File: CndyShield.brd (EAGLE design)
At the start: 69.9 x 78.1 mm, 31 parts, among them U1 ARDUINOR3-BPLACE

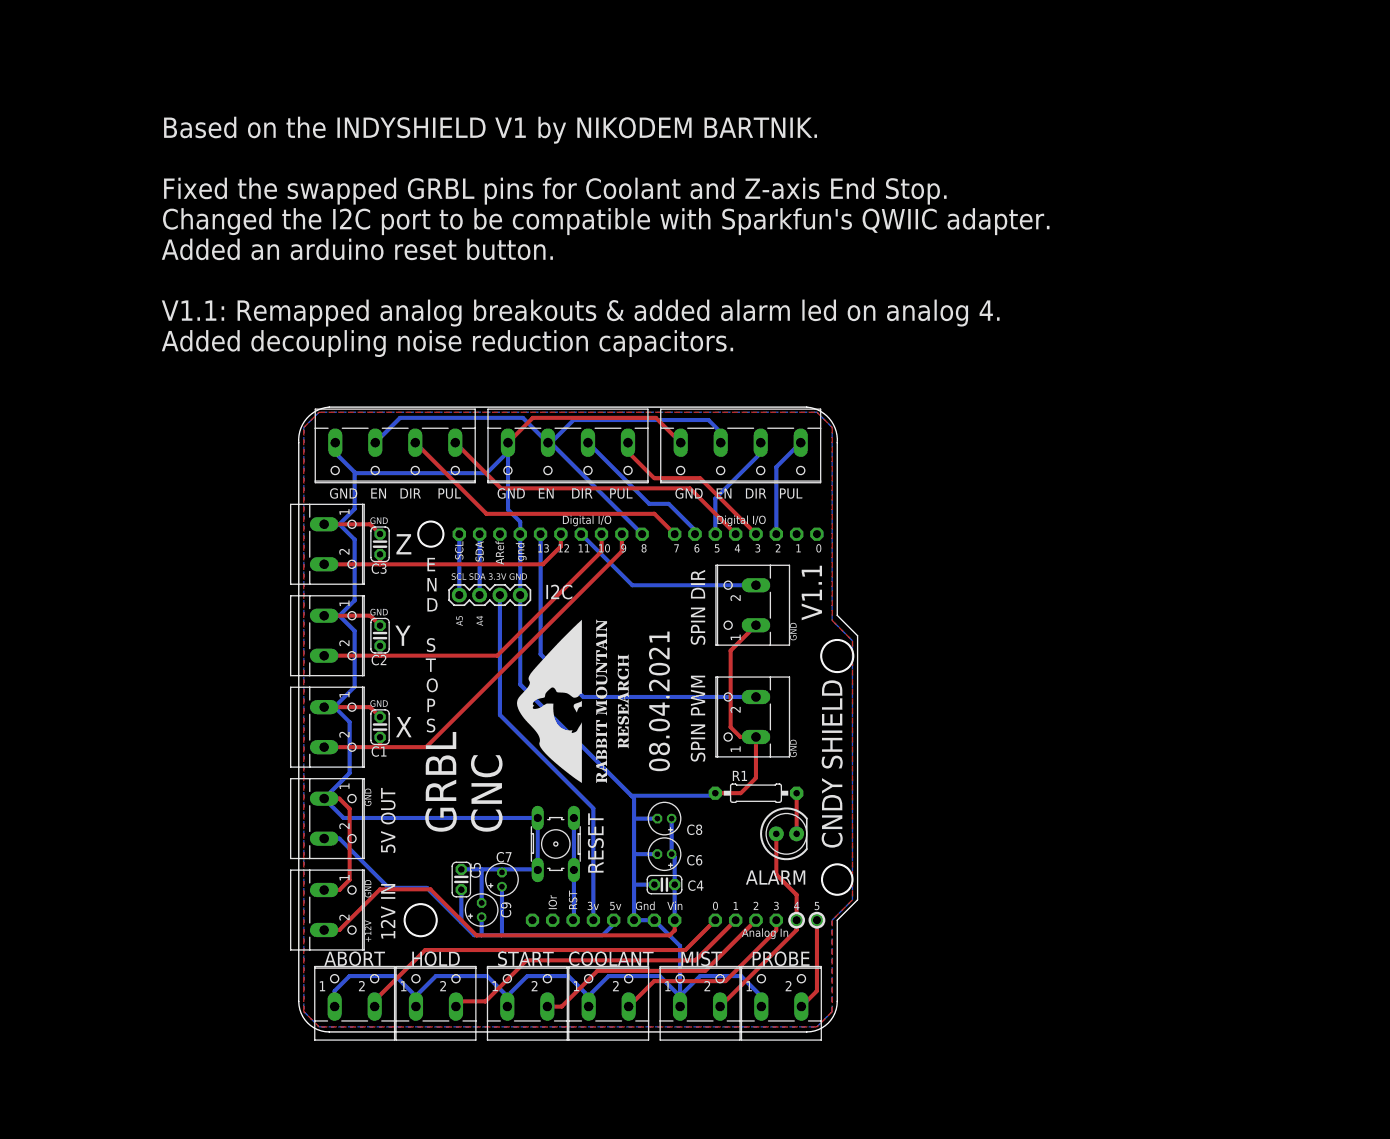
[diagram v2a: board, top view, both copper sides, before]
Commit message: Add files via upload
V1.2: Fixed swapped silkscreen text for Spindle PWM and Spindle Direction. Added optional LED to Spindle PWM (pin 11) as an optional safety warning light.
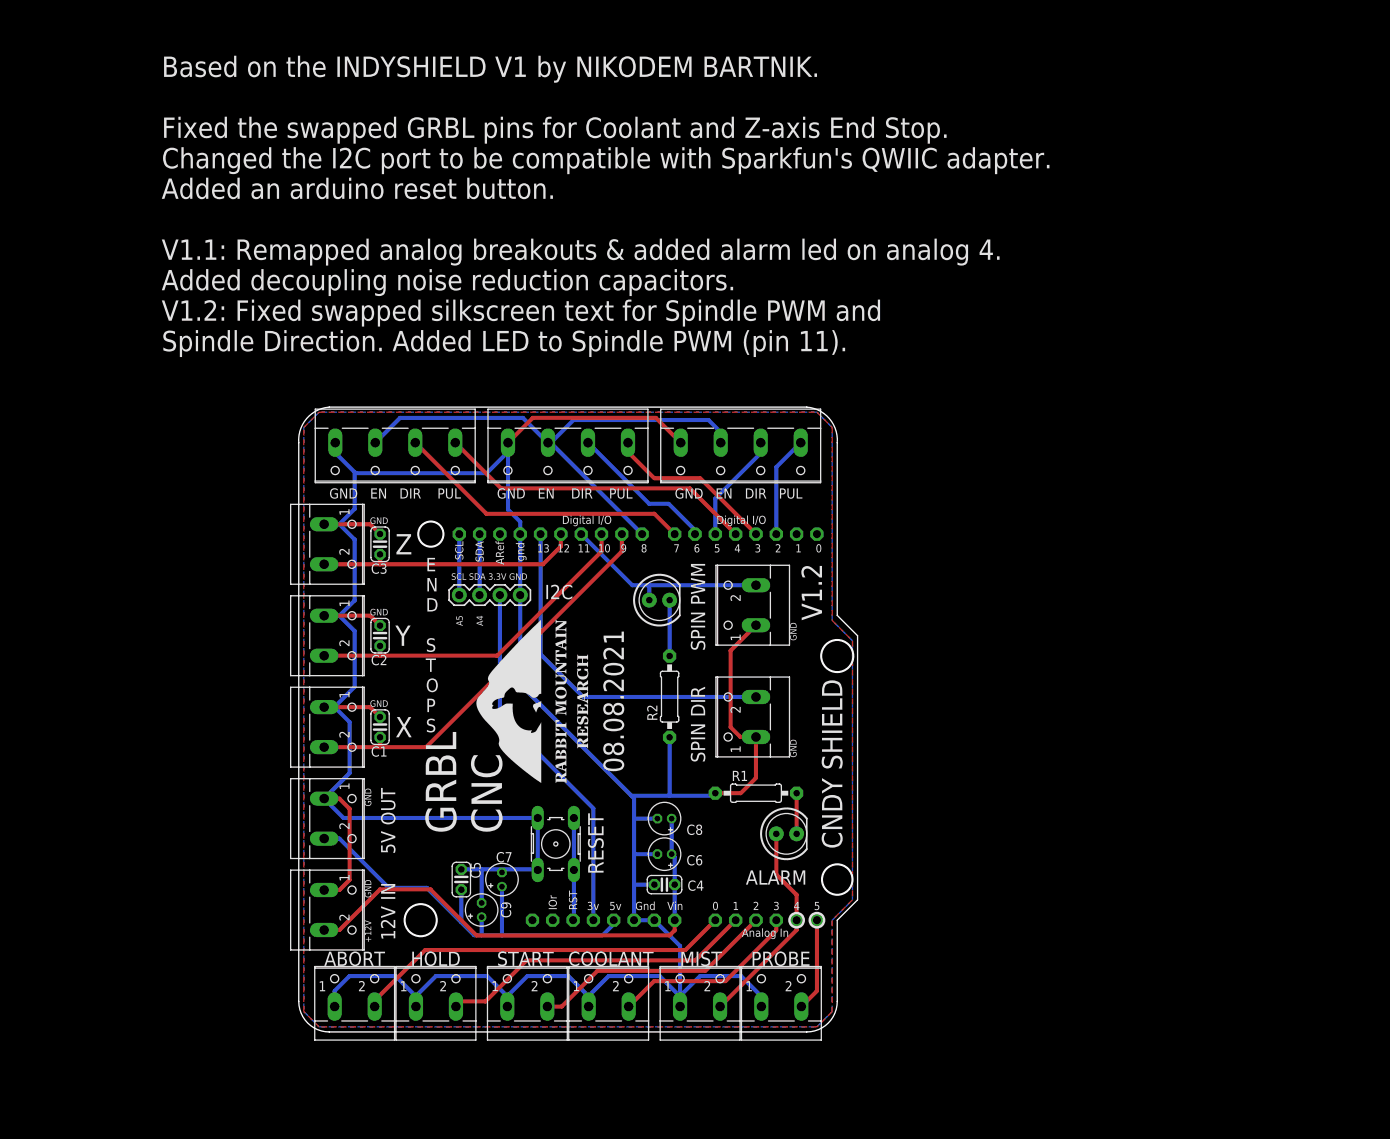
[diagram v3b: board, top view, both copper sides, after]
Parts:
- added D2: (no value), SparkFun-LED:LED_5MM
- added R2: 330, adafruit:0207/10
- moved U$2 5.08 mm to (71.8, 42.5)
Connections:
- new net N$11: D2.K, R2.2
- net GND: now also R2.1
- net SPIN_E: now also D2.A
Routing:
- net GND: track 395.3 -> 402.6 mm
- net N$11: track 0.00 -> 6.98 mm
- net SPIN_E: track 24.5 -> 26.4 mm
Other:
- board text added: "08.08.2021"
- board text added: "Based on the INDYSHIELD V1 by NIKODEM BARTNIK. Fixed the swapped GRBL pins for Coolant and Z-axis End Stop. Changed the I2C port to be compatible with Sparkfun's QWIIC adapter. Added an arduino reset button. V1.1: Remapped analog breakouts & added alarm led on analog 4. Added decoupling noise reduction capacitors. V1.2: Fixed swapped silkscreen text for Spindle PWM and Spindle Direction. Added LE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"
- board text added: "V1.2"
- board text removed: "08.04.2021"
- board text removed: "Based on the INDYSHIELD V1 by NIKODEM BARTNIK. Fixed the swapped GRBL pins for Coolant and Z-axis End Stop. Changed the I2C port to be compatible with Sparkfun's QWIIC adapter. Added an arduino reset button. V1.1: Remapped analog breakouts & added alarm led on analog 4. Added decoupling noise reduction capacitors."
- board text removed: "V1.1"
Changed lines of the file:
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@@
 Added an arduino reset button.
 V1.1: Remapped analog breakouts &amp; added alarm led on analog 4.
-Added decoupling noise reduction capacitors.</text>
-<text x="81.915" y="43.815" size="2.54" layer="25" rot="R90">08.04.2021</text>
+Added decoupling noise reduction capacitors.
+V1.2: Fixed swapped silkscreen text for Spindle PWM and
+Spindle Direction. Added LED to Spindle PWM (pin 11).</text>
+<text x="76.2" y="43.815" size="2.54" layer="25" rot="R90">08.08.2021</text>
 <text x="97.79" y="45.72" size="0.8128" layer="25" rot="R90">GND</text>
 <text x="97.79" y="60.325" size="0.8128" layer="25" rot="R90">GND</text>
@@
 CNC</text>
 <text x="73.66" y="31.115" size="1.9304" layer="21" font="vector" ratio="20" rot="R90">RESET</text>
-<text x="86.36" y="59.69" size="1.778" layer="21" font="vector" ratio="20" rot="R90">SPIN DIR</text>
+<text x="86.36" y="59.055" size="1.778" layer="21" font="vector" ratio="20" rot="R90">SPIN PWM</text>
 <text x="69.215" y="19.685" size="1.778" layer="21" font="vector" ratio="20">COOLANT</text>
 <text x="38.735" y="19.685" size="1.778" layer="21" font="vector" ratio="20">ABORT</text>
-<text x="86.36" y="45.085" size="1.778" layer="21" font="vector" ratio="20" rot="R90">SPIN PWM</text>
+<text x="86.36" y="45.085" size="1.778" layer="21" font="vector" ratio="20" rot="R90">SPIN DIR</text>
 <text x="103.505" y="34.29" size="2.54" layer="21" font="vector" ratio="20" rot="R90">CNDY SHIELD</text>
 <text x="49.53" y="19.685" size="1.778" layer="21" font="vector" ratio="20">HOLD</text>
@@
 <text x="83.185" y="19.685" size="1.778" layer="21" font="vector" ratio="20">MIST</text>
 <text x="92.075" y="19.685" size="1.778" layer="21" font="vector" ratio="20">PROBE</text>
-<text x="100.965" y="62.865" size="2.54" layer="21" font="vector" ratio="20" rot="R90">V1.1</text>
+<text x="100.965" y="62.865" size="2.54" layer="21" font="vector" ratio="20" rot="R90">V1.2</text>
 <text x="47.625" y="22.86" size="1.778" layer="21" font="vector" ratio="20" rot="R90">12V IN</text>
 <text x="47.625" y="33.655" size="1.778" layer="21" font="vector" ratio="20" rot="R90">5V OUT</text>
@@
 <attribute name="VALUE" x="62.611" y="37.973" size="1.27" layer="27" ratio="10" rot="R270"/>
 </element>
-<element name="U$2" library="RMR" package="RMR-SIT-14MM" value="" x="76.835" y="42.545" smashed="yes" rot="R90"/>
+<element name="U$2" library="RMR" package="RMR-SIT-14MM" value="" x="71.755" y="42.545" smashed="yes" rot="R90"/>
 <element name="COOL" library="con-wago-500" library_urn="urn:adsk.eagle:library:195" package="W237-102" package3d_urn="urn:adsk.eagle:package:10688/1" value="" x="74.295" y="15.875" smashed="yes">
 <attribute name="MF" value="" x="63.5" y="38.1" size="1.778" layer="27" display="off"/>
@@
 <attribute name="NAME" x="62.103" y="25.654" size="1.27" layer="25" ratio="10" rot="R90"/>
 <attribute name="VALUE" x="60.198" y="28.829" size="1.27" layer="27" ratio="10" rot="R90"/>
+</element>
+<element name="D2" library="SparkFun-LED" library_urn="urn:adsk.eagle:library:529" package="LED_5MM" package3d_urn="urn:adsk.eagle:package:39353/1" value="" x="80.645" y="65.405" smashed="yes">
+<attribute name="VALUE" x="80.6704" y="62.0141" size="0.6096" layer="27" font="vector" ratio="20" align="top-center"/>
+</element>
+<element name="R2" library="adafruit" library_urn="urn:adsk.eagle:library:420" package="0207/10" package3d_urn="urn:adsk.eagle:package:6240597/1" value="330" x="81.915" y="53.34" smashed="yes" rot="R90">
+<attribute name="NAME" x="80.391" y="50.292" size="1.27" layer="25" ratio="10" rot="R90"/>
+<attribute name="VALUE" x="82.55" y="51.0794" size="1.27" layer="27" ratio="10" rot="R90"/>
 </element>
 </elements>
@@
 <wire x1="83.225" y1="22.185" x2="83.225" y2="14.605" width="0.508" layer="16"/>
 <wire x1="87.63" y1="41.275" x2="87.3125" y2="40.9575" width="0.508" layer="16"/>
-<wire x1="87.3125" y1="40.9575" x2="77.1525" y2="40.9575" width="0.508" layer="16"/>
+<wire x1="87.3125" y1="40.9575" x2="81.915" y2="40.9575" width="0.508" layer="16"/>
 <contactref element="C1" pad="2"/>
 <contactref element="C2" pad="2"/>
 <contactref element="C3" pad="2"/>
+<wire x1="81.915" y1="40.9575" x2="77.1525" y2="40.9575" width="0.508" layer="16"/>
 <wire x1="45.72" y1="73.66" x2="44.49" y2="74.89" width="0.508" layer="1"/>
 <wire x1="44.49" y1="74.89" x2="38.735" y2="74.89" width="0.508" layer="1"/>
@@
 <wire x1="80.391" y1="38.1" x2="77.47" y2="38.1" width="0.508" layer="16"/>
 <wire x1="58.42" y1="27.559" x2="58.42" y2="31.75" width="0.508" layer="16"/>
+<contactref element="R2" pad="1"/>
+<wire x1="81.915" y1="48.26" x2="81.915" y2="40.9575" width="0.508" layer="16"/>
 </signal>
 <signal name="S_EN">
@@
 <contactref element="U1" pad="D11"/>
 <wire x1="77.256" y1="67.27" x2="70.866" y2="73.66" width="0.508" layer="16"/>
-<wire x1="92.71" y1="67.27" x2="77.256" y2="67.27" width="0.508" layer="16"/>
+<wire x1="92.71" y1="67.27" x2="79.375" y2="67.27" width="0.508" layer="16"/>
+<contactref element="D2" pad="A"/>
+<wire x1="79.375" y1="67.27" x2="77.256" y2="67.27" width="0.508" layer="16"/>
+<wire x1="79.375" y1="65.405" x2="79.375" y2="67.27" width="0.508" layer="16"/>
 </signal>
 <signal name="SPIN_DIR">
@@
 <wire x1="97.79" y1="36.195" x2="97.79" y2="41.275" width="0.508" layer="1"/>
 </signal>
+<signal name="N$11">
+<contactref element="D2" pad="K"/>
+<contactref element="R2" pad="2"/>
+<wire x1="81.915" y1="65.405" x2="81.915" y2="58.42" width="0.508" layer="16"/>
+</signal>
 </signals>

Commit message: Add files via upload
V1.3 Updated Silkscreen. Added OSHW Logo. Noise reduction caps.
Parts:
- added C10, C11, C12, C13: (no value), adafruit:C025-024X044
- added U$1: (no value), RMR:OSHW-LOGO-M
- moved U$2 1.42 mm to (73.0, 41.9)
- moved D1 1.27 mm to (96.5, 37.5)
- moved R1 1.27 mm to (92.7, 42.5)
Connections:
- new net MIST: D1.A, U1.A4
- net ABORT: now also C10.1
- net GND: now also C10.2, C11.2, C12.2, C13.2
- net HOLD: now also C11.1
- net LIGHT: no longer D1.A, U1.A4
- net PROBE: now also C13.1
- net START: now also C12.1
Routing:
- net GND: track 402.6 -> 423.0 mm
- net LIGHT: track 26.6 -> 13.5 mm
- net MIST: track 0.00 -> 11.8 mm
- net PROBE: track 11.6 -> 17.1 mm
- net START: track 30.5 -> 35.0 mm
- net HOLD: track 39.8 -> 44.2 mm
- net ABORT: track 47.5 -> 51.9 mm
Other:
- board text added: "Based on the INDYSHIELD V1 by NIKODEM BARTNIK. V1.0: Fixed the swapped GRBL pins for Coolant and Z-axis End Stop. Changed the I2C port to be compatible with Sparkfun's QWIIC adapter. Added an arduino reset button. V1.1: Remapped analog breakouts & added alarm led on analog 4. Added decoupling noise reduction capacitors for limit switches. V1.2: Fixed swapped silkscreen text for Spindle PWM and Sp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"
- board text added: "V1.3"
- board text removed: "A4"
- board text removed: "A5"
- board text removed: "Based on the INDYSHIELD V1 by NIKODEM BARTNIK. Fixed the swapped GRBL pins for Coolant and Z-axis End Stop. Changed the I2C port to be compatible with Sparkfun's QWIIC adapter. Added an arduino reset button. V1.1: Remapped analog breakouts & added alarm led on analog 4. Added decoupling noise reduction capacitors. V1.2: Fixed swapped silkscreen text for Spindle PWM and Spindle Direction. Added LE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"
- board text removed: "SCL SDA 3.3V GND"
- board text removed: "V1.2"
